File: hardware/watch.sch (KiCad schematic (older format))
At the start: 45 parts, among them J1 Conn_01x02_Male, J2 Conn_01x03_Male, J3 Conn_01x01_Male, J4 Conn_01x03_Male, J5 Conn_01x01_Male, SW1 SW_Push, SW2 SW_Push, U1 KCSA02-105, U10 STP08DP05, U11 KCSA02-105, U12 STP08DP05, U13 KCSA02-105, U2 KCSA02-105, U3 STP08DP05, U4 STP08DP05, U5 STM32L011F4Px, U6 TLV70033_SOT23-5, U7 MCP73831-2-OT, U8 LM66100, U9 LM66100, Y1 32kHz

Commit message: working on hardware rev3
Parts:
- removed C1, C16, C2, C5: 100nF, Capacitor_SMD:C_0603_1608Metric_Pad1.05x0.95mm_HandSolder, symbol Device:C_Small
- removed J1: Conn_01x02_Male, Connector_PinHeader_2.54mm:PinHeader_1x02_P2.54mm_Vertical, symbol Connector:Conn_01x02_Male
- removed J2, J4: Conn_01x03_Male, Connector_PinHeader_2.54mm:PinHeader_1x03_P2.54mm_Vertical, symbol Connector:Conn_01x03_Male
- removed J3, J5: Conn_01x01_Male, Connector_PinHeader_2.54mm:PinHeader_1x01_P2.54mm_Vertical, symbol Connector:Conn_01x01_Male
- removed R1, R4, R5: 2k, Resistor_SMD:R_0603_1608Metric_Pad1.05x0.95mm_HandSolder, symbol Device:R_Small
- removed U1, U11, U13, U2: KCSA02-105, Display_7Segment:KCSC02-105, symbol Display_Character:KCSA02-105
- removed U10, U12, U3, U4: STP08DP05, Package_SO:TSSOP-16_4.4x5mm_P0.65mm, symbol Driver_LED:STP08CP05
- removed U8, U9: LM66100, lm66100:LM66100DCKT, symbol watch:LM66100
- added J1: USB_C_Receptacle_USB2.0, Connector_USB:USB_C_Receptacle_Palconn_UTC16-G, symbol Connector:USB_C_Receptacle_USB2.0
- added J2: Conn_01x04_Male, Connector_PinHeader_2.54mm:PinHeader_1x04_P2.54mm_Vertical, symbol Connector:Conn_01x04_Male
- added U3: TPS2115A-Q1, watch:TSSOP-8_3x6.4_P0.65mm, symbol watch:TPS2115A-Q1
- added U?: LM66100, lm66100:LM66100DCKT, symbol watch:LM66100
- R2: value 2k -> 10k; Order https://www.digikey.at/product-detail/de/panasonic-electron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 -> https://www.digikey.at/product-detail/de/te-connectivity-pa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
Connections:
- net labels removed: RX, S1_A, S1_B, S1_C, S1_D, S1_DP, S1_E, S1_F, S1_G, S2_A, S2_B, S2_C, S2_D, S2_DP, S2_E, S2_F, S2_G, S3_A, S3_B, S3_C, S3_D, S3_DP, S3_E, S3_F, S3_G, S4_A, S4_B, S4_C, S4_D, S4_DP, S4_E, S4_F, S4_G, TX
- wire segments 138 -> 97
- no-connect marks 2 -> 4
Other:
- note added: "Input Voltage Connector"
- note added: "TODO:\nChange me!"
- note removed: "LED Driver"
- note removed: "LED-Displays"
- note removed: "USART Interface"

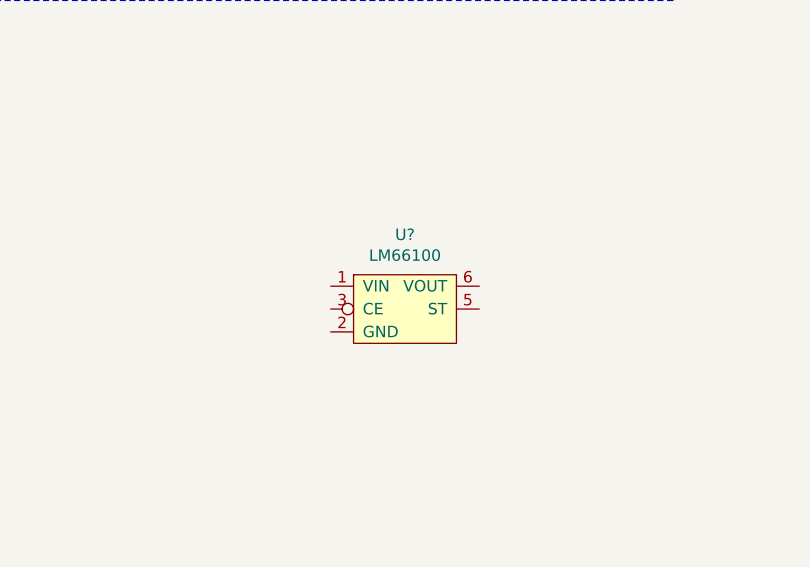
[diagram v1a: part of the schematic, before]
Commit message: reverse current protection
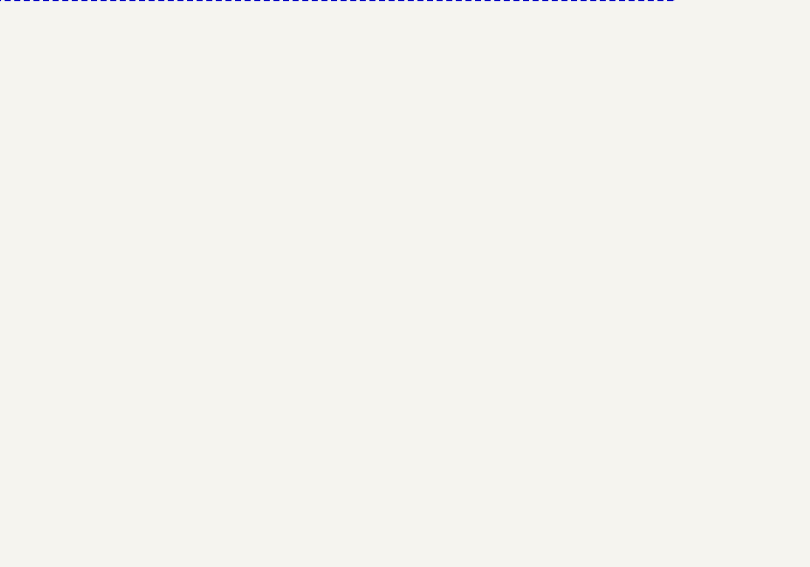
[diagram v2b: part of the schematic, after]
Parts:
- removed U?: LM66100, lm66100:LM66100DCKT, symbol watch:LM66100
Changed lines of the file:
@@
 Wire Notes Line
 	6500 500  6500 2700
-$Comp
-L watch:LM66100 U?
-U 1 1 606F82F9
-P 5300 4100
-F 0 "U?" H 5325 4475 50  0000 C CNN
-F 1 "LM66100" H 5325 4384 50  0000 C CNN
-F 2 "lm66100:LM66100DCKT" H 5250 4400 50  0001 C CNN
-F 3 "" H 5250 4400 50  0001 C CNN
-	1    5300 4100
-	1    0    0    -1
-$EndComp
 $EndSCHEMATC

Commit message: hardware development
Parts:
- removed BT1: Battery_Cell, Connector_PinHeader_2.54mm:PinHeader_1x02_P2.54mm_Vertical, symbol Device:Battery_Cell
- removed C14, C3: 10uF, Capacitor_SMD:C_0603_1608Metric_Pad1.05x0.95mm_HandSolder, symbol Device:C_Small
- removed R3: 3k9, Resistor_SMD:R_0603_1608Metric_Pad1.05x0.95mm_HandSolder, symbol Device:R_Small
- removed R6, R7: 47k, Resistor_SMD:R_0603_1608Metric_Pad1.05x0.95mm_HandSolder, symbol Device:R_Small
- removed U7: MCP73831-2-OT, Package_TO_SOT_SMD:SOT-23-5, symbol Battery_Management:MCP73831-2-OT
- added C? (x2): 100nF, Capacitor_SMD:C_0603_1608Metric_Pad1.05x0.95mm_HandSolder, symbol Device:C_Small
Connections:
- net GND: now also C?.2, C?.2
- net +5V renamed Battery Charger/VIN
- net Battery Charger/VIN: now also C?.1
- net +BATT renamed Battery Charger/VBAT
- net Battery Charger/VBAT: now also C?.1
- no-connect marks 4 -> 8
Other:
- note removed: "Bat LVL"
- note removed: "Battery Charger"
- note removed: "Input Power Selection"
- note removed: "TODO:\nChange me!"
- moved on the sheet: C15, C4, R2, U3, U6

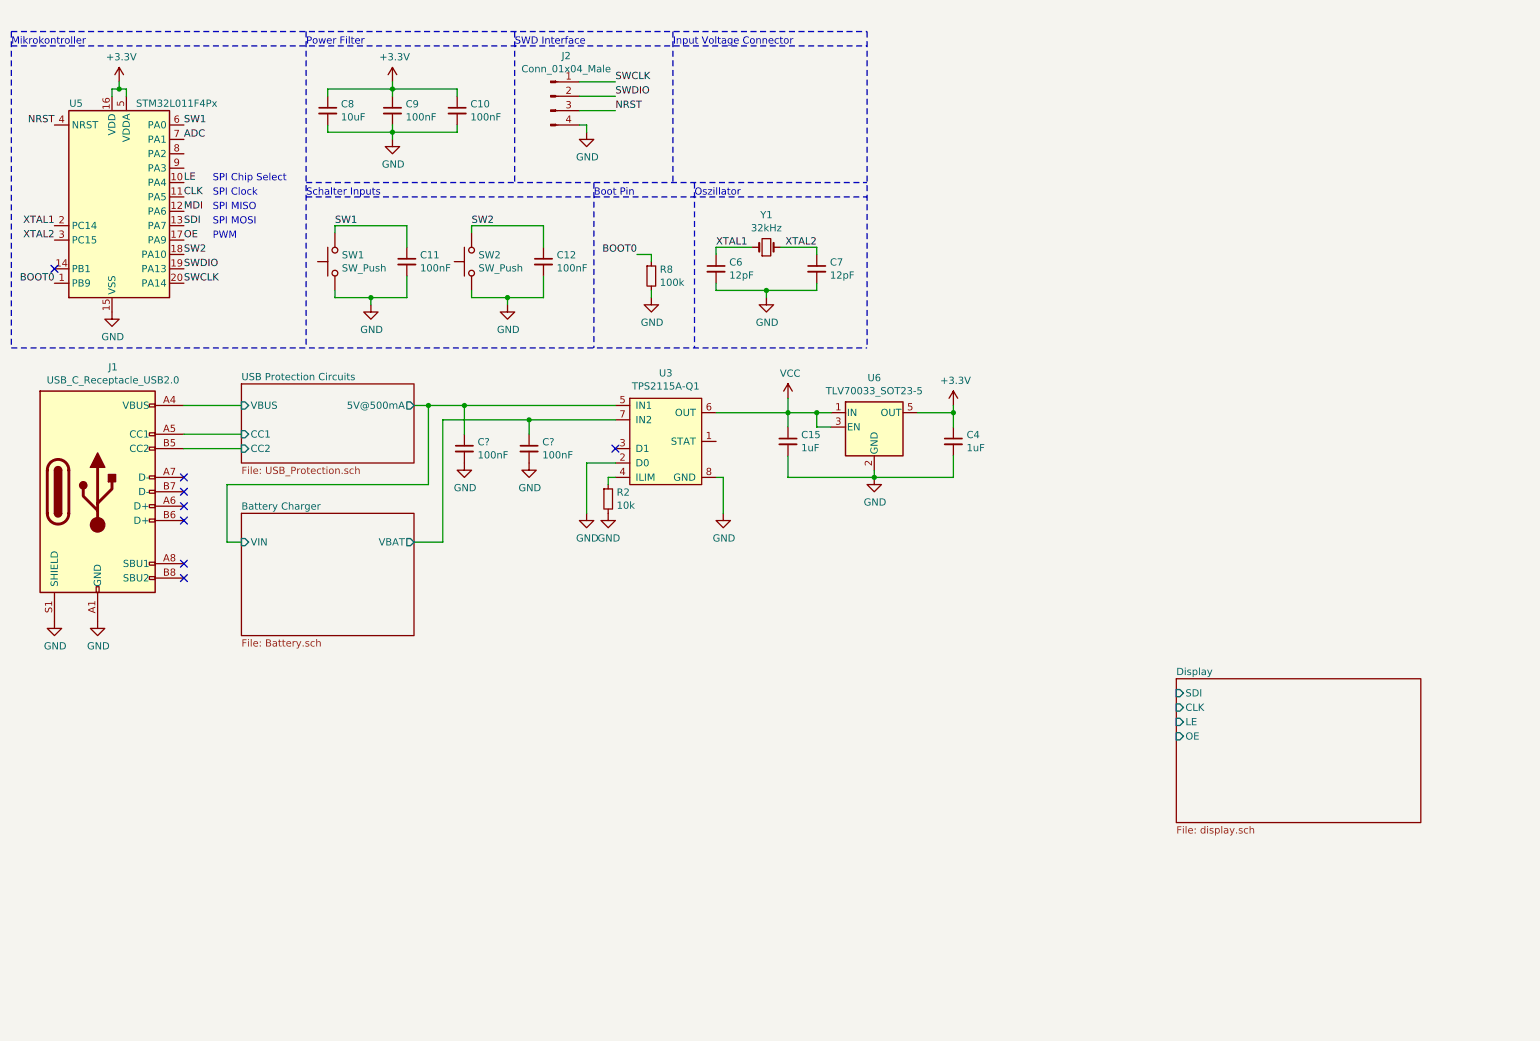
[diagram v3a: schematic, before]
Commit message: schematic should be done, pcb is next
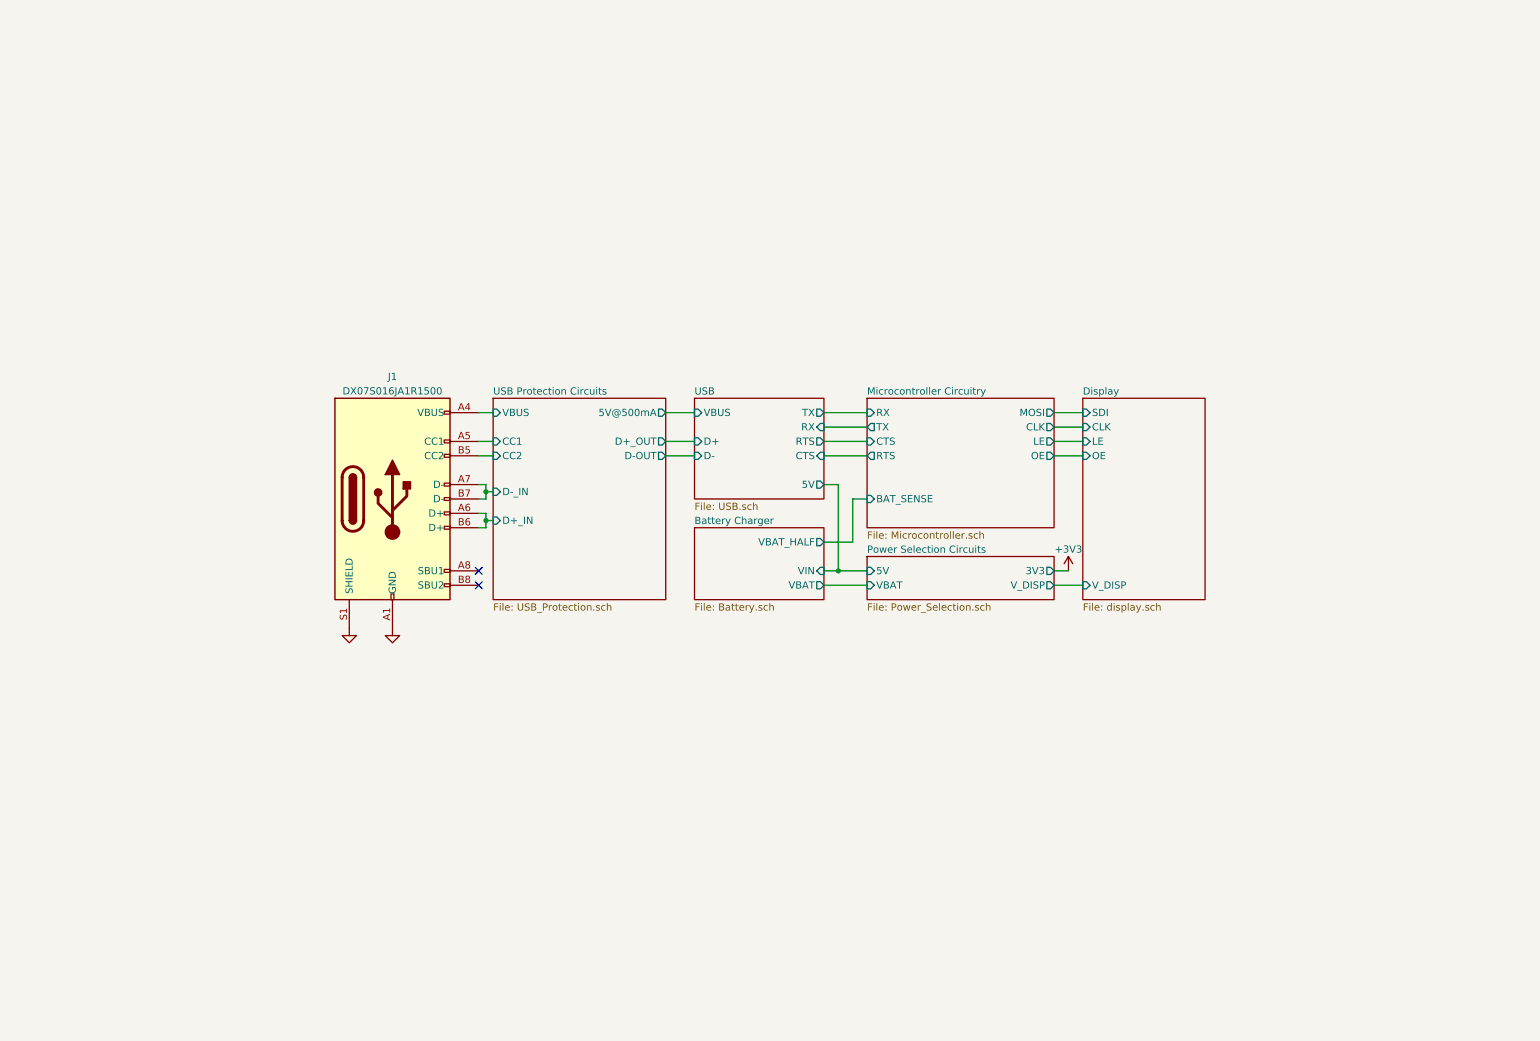
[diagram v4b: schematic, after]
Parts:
- removed C10, C11, C12, C9, C? (x2): 100nF, Capacitor_SMD:C_0603_1608Metric_Pad1.05x0.95mm_HandSolder, symbol Device:C_Small
- removed C15, C4: 1uF, Capacitor_SMD:C_0603_1608Metric_Pad1.05x0.95mm_HandSolder, symbol Device:C_Small
- removed C6, C7: 12pF, Capacitor_SMD:C_0603_1608Metric_Pad1.05x0.95mm_HandSolder, symbol Device:C_Small
- removed C8: 10uF, Capacitor_SMD:C_0603_1608Metric_Pad1.05x0.95mm_HandSolder, symbol Device:C_Small
- removed J2: Conn_01x04_Male, Connector_PinHeader_2.54mm:PinHeader_1x04_P2.54mm_Vertical, symbol Connector:Conn_01x04_Male
- removed R2: 10k, Resistor_SMD:R_0603_1608Metric_Pad1.05x0.95mm_HandSolder, symbol Device:R_Small
- removed R8: 100k, Resistor_SMD:R_0603_1608Metric_Pad1.05x0.95mm_HandSolder, symbol Device:R_Small
- removed SW1, SW2: SW_Push, Button_Switch_SMD:SW_Push_1P1T_NO_CK_KMR2, symbol Switch:SW_Push
- removed U3: TPS2115A-Q1, watch:TSSOP-8_3x6.4_P0.65mm, symbol watch:TPS2115A-Q1
- removed U5: STM32L011F4Px, Package_SO:TSSOP-20_4.4x6.5mm_P0.65mm, symbol MCU_ST_STM32L0:STM32L011F4Px
- removed U6: TLV70033_SOT23-5, Package_TO_SOT_SMD:SOT-23-5, symbol Regulator_Linear:TLV70033_SOT23-5
- removed Y1: 32kHz, Crystal:Crystal_SMD_3215-2Pin_3.2x1.5mm, symbol Device:Crystal_Small
- J1: value USB_C_Receptacle_USB2.0 -> DX07S016JA1R1500; footprint Connector_USB:USB_C_Receptacle_Palconn_UTC16-G -> watch:DX07S016JA1R1500; Manufacturer (none) -> JAE Electronics; Order (none) -> https://www.mouser.at/ProductDetail/JAE-Electronics/DX07S01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
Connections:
- net USB Protection Circuits/D+_IN: now reaches J1.A6 (D+)
- net USB Protection Circuits/D+_IN: now also J1.B6 (D+)
- net USB Protection Circuits/D-_IN: now reaches J1.A7 (D-)
- net USB Protection Circuits/D-_IN: now also J1.B7 (D-)
- no-connect marks 8 -> 2
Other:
- note removed: "Boot Pin"
- note removed: "Input Voltage Connector"
- note removed: "Mikrokontroller"
- note removed: "Oszillator"
- note removed: "PWM"
- note removed: "Power Filter"
- note removed: "SPI Chip Select"
- note removed: "SPI Clock"
- note removed: "SPI MISO"
- note removed: "SPI MOSI"
- note removed: "SWD Interface"
- note removed: "Schalter Inputs"
- moved on the sheet: J1
